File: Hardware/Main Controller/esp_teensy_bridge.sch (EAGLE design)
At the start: 42 parts, among them IC1 BQ79600PWRQ1, Q1 SI7611DN-T1-GE3, Q2 SI7611DN-T1-GE3, Q3 SI7611DN-T1-GE3, Q4 SI7611DN-T1-GE3

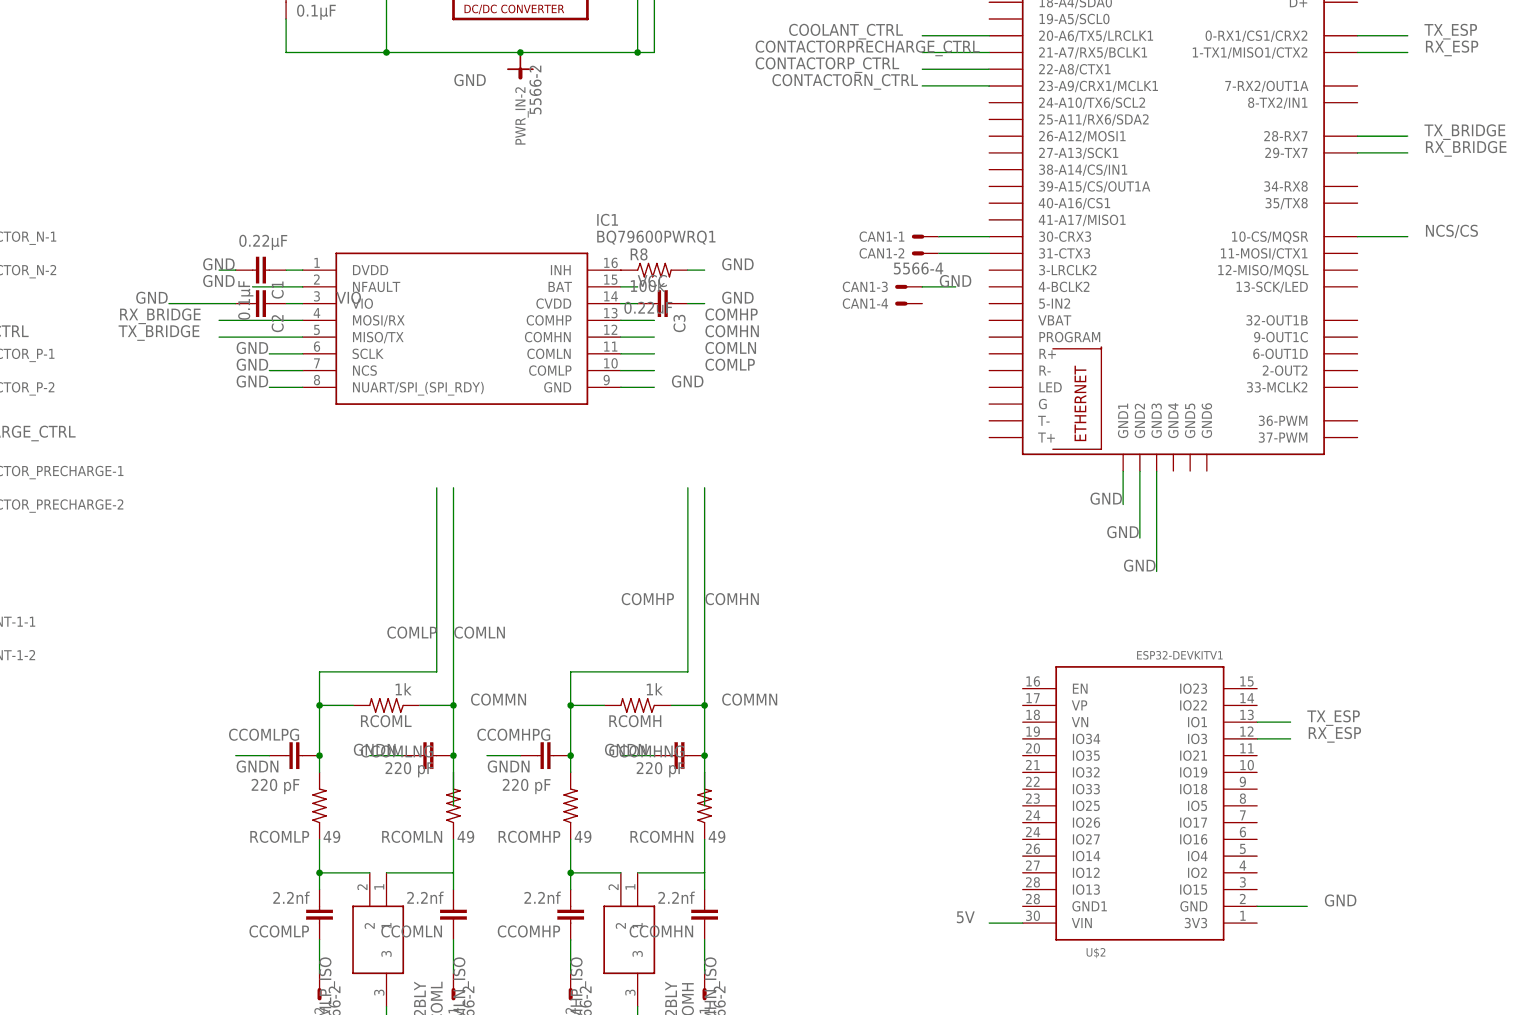
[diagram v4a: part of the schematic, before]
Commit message: change from uart to spi
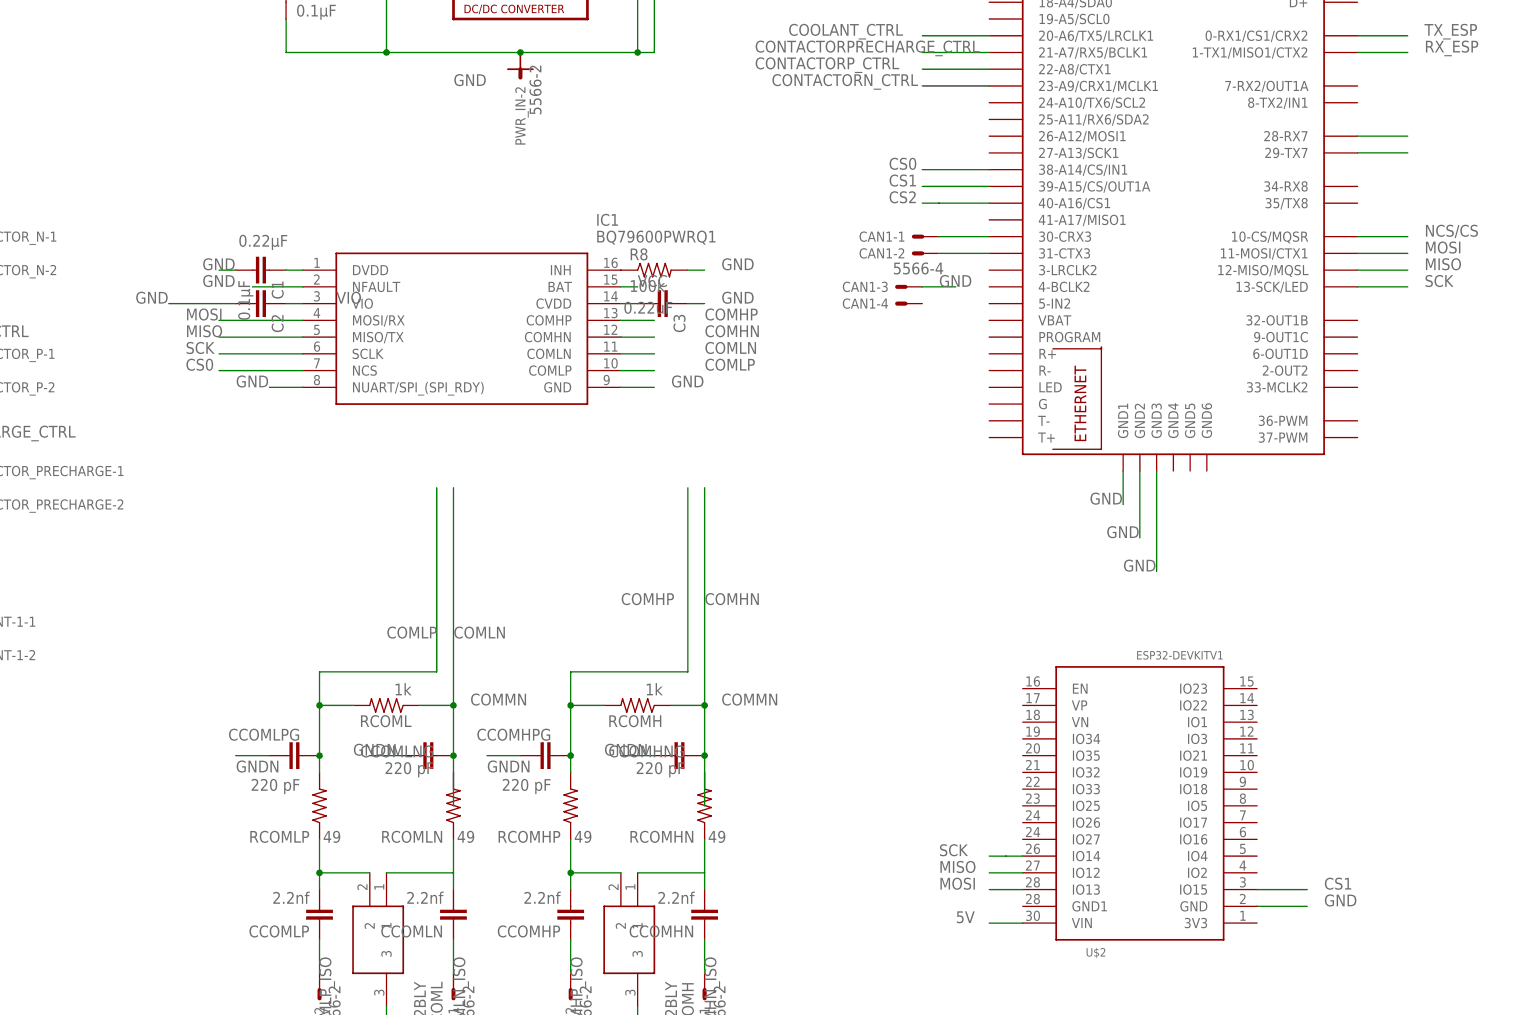
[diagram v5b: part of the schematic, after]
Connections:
- new net CS0: IC1.NCS, U$3.38-A14/CS/IN1
- new net CS1: U$2.IO15, U$3.39-A15/CS/OUT1A
- new net CS2: U$3.40-A16/CS1
- new net MISO: IC1.MISO/TX, U$2.IO12, U$3.12-MISO/MQSL
- new net MOSI: IC1.MOSI/RX, U$2.IO13, U$3.11-MOSI/CTX1
- new net SCK: IC1.SCLK, U$2.IO14, U$3.13-SCK/LED
- net GND: no longer IC1.NCS, IC1.SCLK
- net RX_BRIDGE: no longer IC1.MOSI/RX
- net RX_ESP: no longer U$2.IO3
- net TX_BRIDGE: no longer IC1.MISO/TX
- net TX_ESP: no longer U$2.IO1
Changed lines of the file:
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@@
-</segment>
-<segment>
-<pinref part="IC1" gate="G$1" pin="SCLK"/>
-<wire x1="-63.5" y1="53.34" x2="-68.58" y2="53.34" width="0.1524" layer="91"/>
-<label x="-73.66" y="53.34" size="1.778" layer="95"/>
 </segment>
 <segment>
@@
 <wire x1="-63.5" y1="48.26" x2="-68.58" y2="48.26" width="0.1524" layer="91"/>
 <label x="-73.66" y="48.26" size="1.778" layer="95"/>
-</segment>
-<segment>
-<pinref part="IC1" gate="G$1" pin="NCS"/>
-<wire x1="-63.5" y1="50.8" x2="-68.58" y2="50.8" width="0.1524" layer="91"/>
-<label x="-73.66" y="50.8" size="1.778" layer="95"/>
 </segment>
 <segment>
@@
 <net name="TX_ESP" class="0">
 <segment>
-<pinref part="U$2" gate="G$1" pin="IO1"/>
-<wire x1="81.28" y1="-2.54" x2="86.36" y2="-2.54" width="0.1524" layer="91"/>
-<label x="88.9" y="-2.54" size="1.778" layer="95"/>
-</segment>
-<segment>
 <pinref part="U$3" gate="G$1" pin="0-RX1/CS1/CRX2"/>
 <wire x1="96.52" y1="101.6" x2="104.14" y2="101.6" width="0.1524" layer="91"/>
@@
 <net name="RX_ESP" class="0">
 <segment>
-<pinref part="U$2" gate="G$1" pin="IO3"/>
-<wire x1="81.28" y1="-5.08" x2="86.36" y2="-5.08" width="0.1524" layer="91"/>
-<label x="88.9" y="-5.08" size="1.778" layer="95"/>
-</segment>
-<segment>
 <pinref part="U$3" gate="G$1" pin="1-TX1/MISO1/CTX2"/>
 <wire x1="96.52" y1="99.06" x2="104.14" y2="99.06" width="0.1524" layer="91"/>
@@
 <net name="TX_BRIDGE" class="0">
 <segment>
-<pinref part="IC1" gate="G$1" pin="MISO/TX"/>
-<wire x1="-63.5" y1="55.88" x2="-76.2" y2="55.88" width="0.1524" layer="91"/>
-<label x="-91.44" y="55.88" size="1.778" layer="95"/>
-</segment>
-<segment>
 <pinref part="U$3" gate="G$1" pin="28-RX7"/>
 <wire x1="96.52" y1="86.36" x2="104.14" y2="86.36" width="0.1524" layer="91"/>
-<label x="106.68" y="86.36" size="1.778" layer="95"/>
 </segment>
 </net>
 <net name="RX_BRIDGE" class="0">
-<segment>
-<pinref part="IC1" gate="G$1" pin="MOSI/RX"/>
-<wire x1="-63.5" y1="58.42" x2="-76.2" y2="58.42" width="0.1524" layer="91"/>
-<label x="-91.44" y="58.42" size="1.778" layer="95"/>
-</segment>
 <segment>
 <pinref part="U$3" gate="G$1" pin="29-TX7"/>
 <wire x1="96.52" y1="83.82" x2="104.14" y2="83.82" width="0.1524" layer="91"/>
-<label x="106.68" y="83.82" size="1.778" layer="95"/>
 </segment>
 </net>
@@
 </segment>
 </net>
+<net name="MOSI" class="0">
+<segment>
+<pinref part="IC1" gate="G$1" pin="MOSI/RX"/>
+<wire x1="-63.5" y1="58.42" x2="-76.2" y2="58.42" width="0.1524" layer="91"/>
+<label x="-81.28" y="58.42" size="1.778" layer="95"/>
+</segment>
+<segment>
+<pinref part="U$3" gate="G$1" pin="11-MOSI/CTX1"/>
+<wire x1="96.52" y1="68.58" x2="104.14" y2="68.58" width="0.1524" layer="91"/>
+<label x="106.68" y="68.58" size="1.778" layer="95"/>
+</segment>
+<segment>
+<pinref part="U$2" gate="G$1" pin="IO13"/>
+<wire x1="45.72" y1="-27.94" x2="40.64" y2="-27.94" width="0.1524" layer="91"/>
+<label x="33.02" y="-27.94" size="1.778" layer="95"/>
+</segment>
+</net>
+<net name="MISO" class="0">
+<segment>
+<pinref part="IC1" gate="G$1" pin="MISO/TX"/>
+<wire x1="-63.5" y1="55.88" x2="-76.2" y2="55.88" width="0.1524" layer="91"/>
+<label x="-81.28" y="55.88" size="1.778" layer="95"/>
+</segment>
+<segment>
+<pinref part="U$3" gate="G$1" pin="12-MISO/MQSL"/>
+<wire x1="96.52" y1="66.04" x2="104.14" y2="66.04" width="0.1524" layer="91"/>
+<label x="106.68" y="66.04" size="1.778" layer="95"/>
+</segment>
+<segment>
+<pinref part="U$2" gate="G$1" pin="IO12"/>
+<wire x1="45.72" y1="-25.4" x2="40.64" y2="-25.4" width="0.1524" layer="91"/>
+<label x="33.02" y="-25.4" size="1.778" layer="95"/>
+</segment>
+</net>
+<net name="SCK" class="0">
+<segment>
+<pinref part="IC1" gate="G$1" pin="SCLK"/>
+<wire x1="-63.5" y1="53.34" x2="-76.2" y2="53.34" width="0.1524" layer="91"/>
+<label x="-81.28" y="53.34" size="1.778" layer="95"/>
+</segment>
+<segment>
+<pinref part="U$3" gate="G$1" pin="13-SCK/LED"/>
+<wire x1="96.52" y1="63.5" x2="104.14" y2="63.5" width="0.1524" layer="91"/>
+<label x="106.68" y="63.5" size="1.778" layer="95"/>
+</segment>
+<segment>
+<pinref part="U$2" gate="G$1" pin="IO14"/>
+<wire x1="45.72" y1="-22.86" x2="43.18" y2="-22.86" width="0.1524" layer="91"/>
+<wire x1="40.64" y1="-22.86" x2="43.18" y2="-22.86" width="0.1524" layer="91"/>
+<label x="33.02" y="-22.86" size="1.778" layer="95"/>
+</segment>
+</net>
+<net name="CS2" class="0">
+<segment>
+<pinref part="U$3" gate="G$1" pin="40-A16/CS1"/>
+<wire x1="40.64" y1="76.2" x2="33.02" y2="76.2" width="0.1524" layer="91"/>
+<wire x1="30.48" y1="76.2" x2="33.02" y2="76.2" width="0.1524" layer="91"/>
+<label x="25.4" y="76.2" size="1.778" layer="95"/>
+</segment>
+</net>
+<net name="CS1" class="0">
+<segment>
+<pinref part="U$3" gate="G$1" pin="39-A15/CS/OUT1A"/>
+<wire x1="40.64" y1="78.74" x2="30.48" y2="78.74" width="0.1524" layer="91"/>
+<label x="25.4" y="78.74" size="1.778" layer="95"/>
+</segment>
+<segment>
+<pinref part="U$2" gate="G$1" pin="IO15"/>
+<wire x1="81.28" y1="-27.94" x2="88.9" y2="-27.94" width="0.1524" layer="91"/>
+<label x="91.44" y="-27.94" size="1.778" layer="95"/>
+</segment>
+</net>
+<net name="CS0" class="0">
+<segment>
+<pinref part="U$3" gate="G$1" pin="38-A14/CS/IN1"/>
+<wire x1="40.64" y1="81.28" x2="30.48" y2="81.28" width="0.1524" layer="91"/>
+<label x="25.4" y="81.28" size="1.778" layer="95"/>
+</segment>
+<segment>
+<pinref part="IC1" gate="G$1" pin="NCS"/>
+<wire x1="-63.5" y1="50.8" x2="-76.2" y2="50.8" width="0.1524" layer="91"/>
+<label x="-81.28" y="50.8" size="1.778" layer="95"/>
+</segment>
+</net>

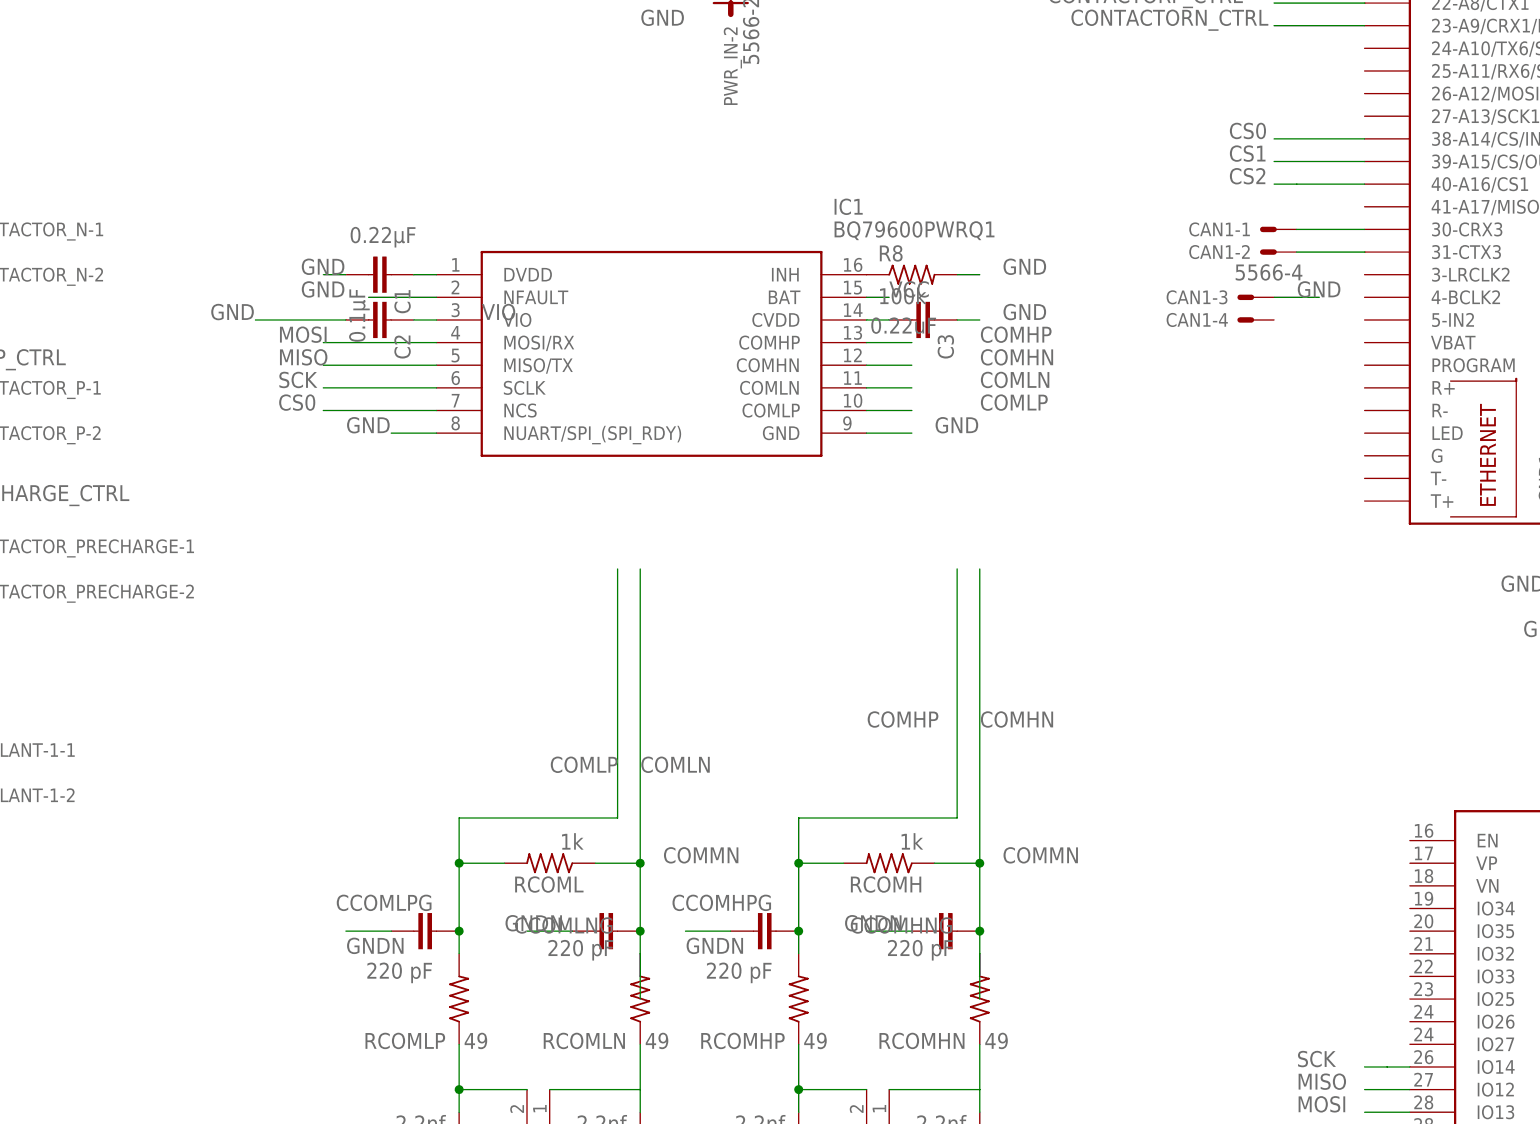
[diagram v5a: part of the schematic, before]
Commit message: Mainboard routing
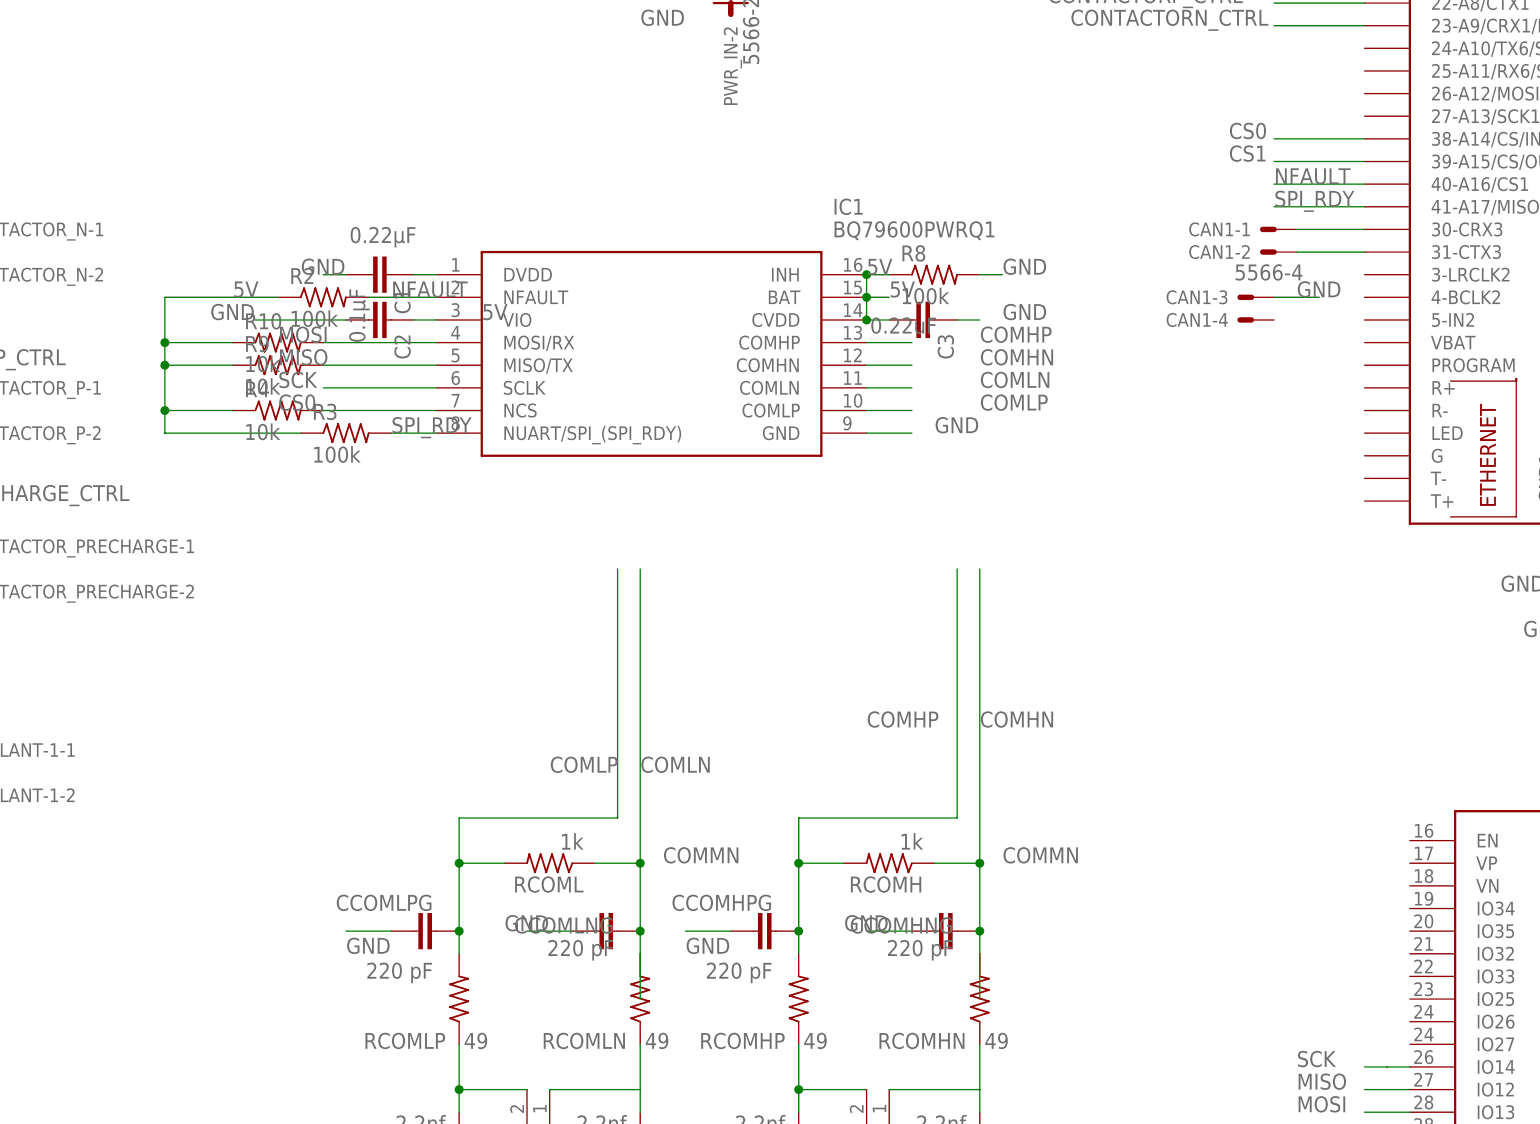
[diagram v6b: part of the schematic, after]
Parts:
- added R10, R4, R9: 10k, rcl:R-US_R0603
- added R2, R3: 100k, rcl:R-US_R0603
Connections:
- removed net CS2: U$3.40-A16/CS1
- removed net GNDN: CCOMHNG.1, CCOMHPG.1, CCOMLNG.1, CCOMLPG.1
- removed net N$3: C3.2, IC1.CVDD
- removed net N$4: IC1.INH, R8.1
- removed net VIO: C2.1, IC1.VIO
- new net NFAULT: IC1.NFAULT, R2.2, U$3.40-A16/CS1
- new net SPI_RDY: IC1.NUART/SPI_(SPI_RDY), R3.2, U$3.41-A17/MISO1
- net 5V: now also C2.1, C3.2, IC1.BAT, IC1.CVDD, IC1.INH, IC1.VIO, R10.1, R2.1, R3.1, R4.1, R8.1, R9.1
- net CS0: now also R4.2
- net GND: now also CCOMHNG.1, CCOMHPG.1, CCOMLNG.1, CCOMLPG.1; no longer IC1.NFAULT, IC1.NUART/SPI_(SPI_RDY)
- net MISO: now also R9.2
- net MOSI: now also R10.2
- net VCC: no longer IC1.BAT
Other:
- moved on the sheet: R8

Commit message: design review changes
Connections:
- net RX_ESP: now also U$2.IO3
- net TX_ESP: now also U$2.IO1
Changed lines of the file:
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@@
 <label x="106.68" y="101.6" size="1.778" layer="95"/>
+</segment>
+<segment>
+<pinref part="U$2" gate="G$1" pin="IO1"/>
+<wire x1="81.28" y1="-2.54" x2="88.9" y2="-2.54" width="0.1524" layer="91"/>
+<label x="91.44" y="-2.54" size="1.778" layer="95"/>
 </segment>
 </net>
@@
 <label x="106.68" y="99.06" size="1.778" layer="95"/>
 </segment>
+<segment>
+<pinref part="U$2" gate="G$1" pin="IO3"/>
+<wire x1="81.28" y1="-5.08" x2="88.9" y2="-5.08" width="0.1524" layer="91"/>
+<label x="91.44" y="-5.08" size="1.778" layer="95"/>
+</segment>
 </net>
